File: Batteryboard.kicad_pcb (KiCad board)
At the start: 2 copper layers, 128.9 x 70.5 mm, 76 parts, among them J1 Conn_01x02_Male, J2 Conn_01x03_Male, J3 Conn_01x02_Male, J4 Conn_01x02_Male, Q1 SI7617DN-T1-GE3, Q2 SI7617DN-T1-GE3, Q3 SI7617DN-T1-GE3, Q4 SIS412DN-T1-GE3, Q5 SIS412DN-T1-GE3, Q6 SIS412DN-T1-GE3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

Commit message: needed to use a different cap, cause the value wasnt on digikey
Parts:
- CTTC1: value 43nF -> 47nF
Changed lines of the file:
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@@
   )
   (setup
-    (last_trace_width 0.762)
+    (last_trace_width 0.25)
     (user_trace_width 0.2794)
     (user_trace_width 0.3048)
@@
       (effects (font (size 1 1) (thickness 0.15)))
     )
-    (fp_text value 43nF (at 0 1.82) (layer F.Fab)
-      (effects (font (size 1 1) (thickness 0.15)))
-    )
+    (fp_text value 47nF (at 0 1.82) (layer F.Fab)
+      (effects (font (size 1 1) (thickness 0.15)))
+    )

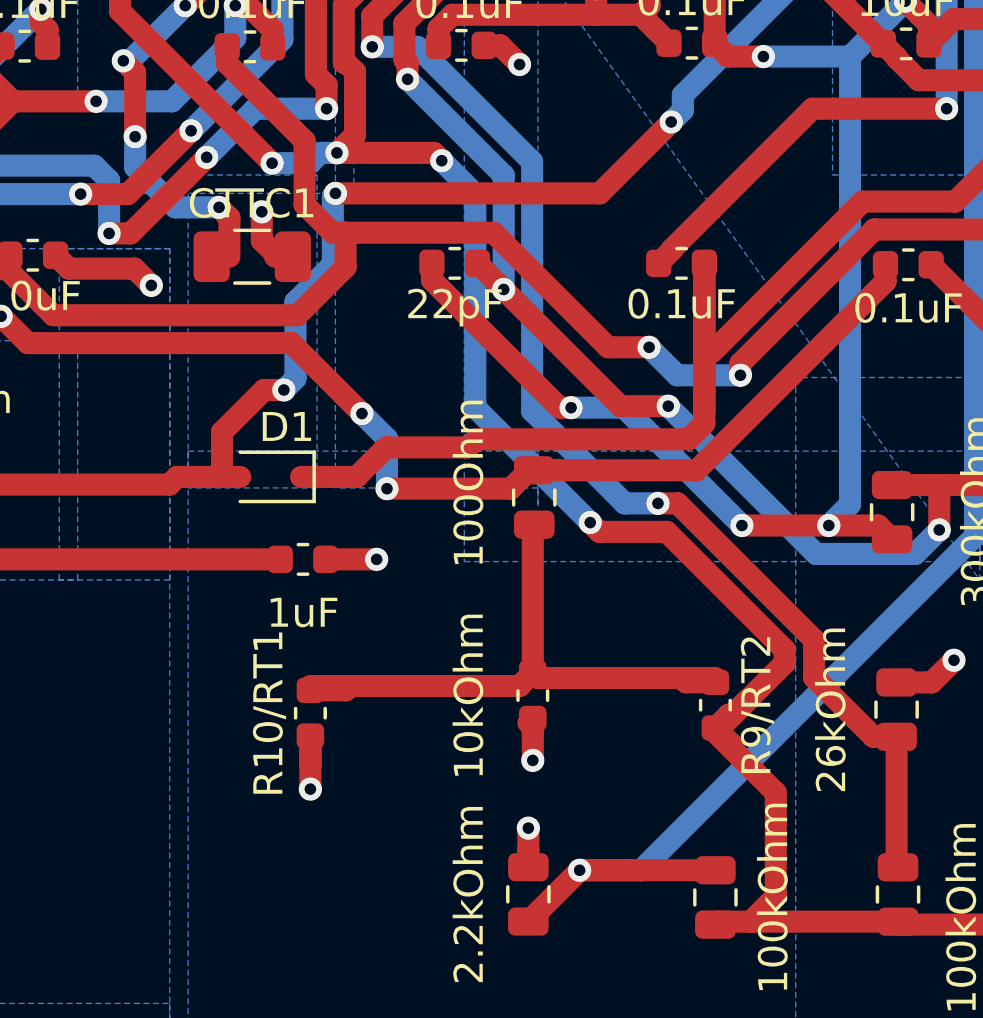
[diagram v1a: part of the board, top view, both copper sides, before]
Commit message: fixed some footprints
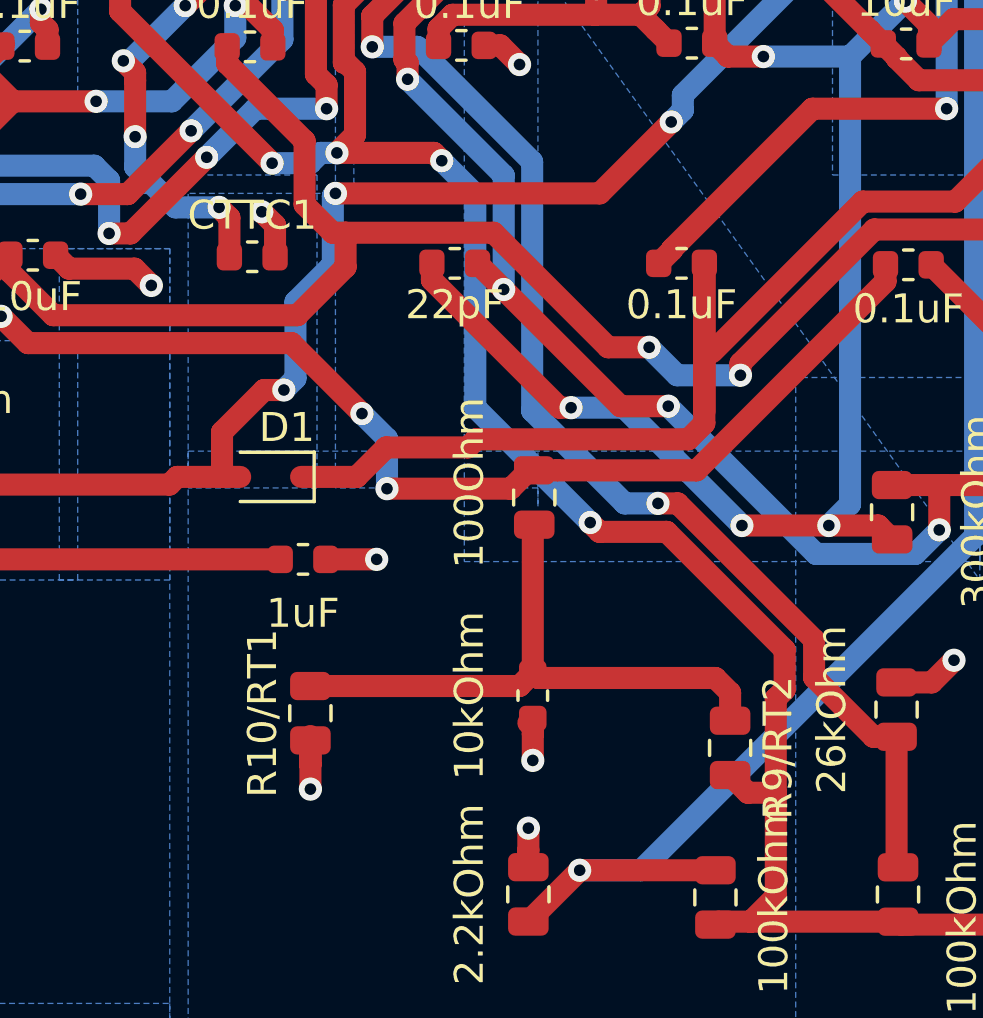
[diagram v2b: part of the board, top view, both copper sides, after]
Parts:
- CTTC1: footprint Capacitor_SMD:C_1206_3216Metric -> Capacitor_SMD:C_0603_1608Metric
- R10/RT1, R9/RT2: footprint Resistor_SMD:R_0603_1608Metric -> Resistor_SMD:R_0805_2012Metric
- moved R9/RT2 1.56 mm to (133.0, 139.1)
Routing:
- net Net-(C4-Pad1): track 93.2 -> 90.9 mm
- net Net-(NTCTH1/NTCG163JF103FT1S1-Pad2): track 22.0 -> 21.0 mm
